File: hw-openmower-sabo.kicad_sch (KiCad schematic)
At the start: 31 parts, among them J1 Conn_01x05_Pin, J19 Conn_01x02, J20 Conn_01x02, J31 Conn_01x03_Pin, J32 Conn_02x08_Odd_Even, J33 Molex 470531000, M1 Fan, M2 Fan, Q4 AO3400A, Q5 AO3400A, U44 INA293A1, U7 M24C02-WMN

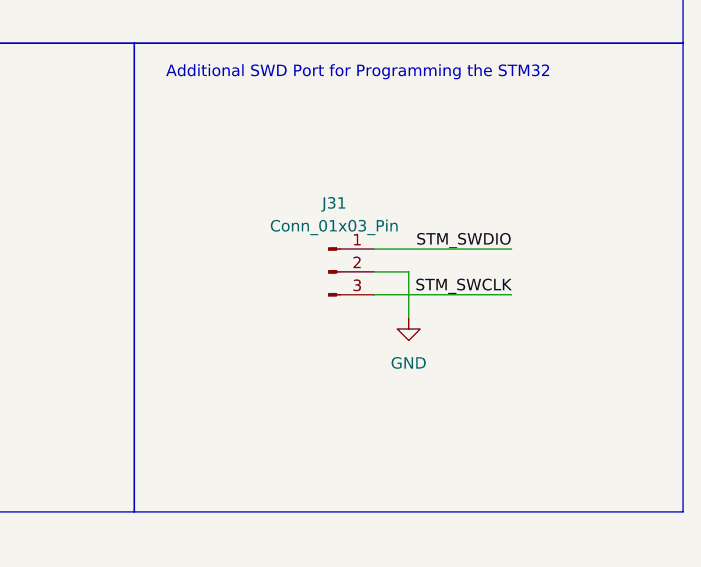
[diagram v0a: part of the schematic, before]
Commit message: - Increase charger Vfb
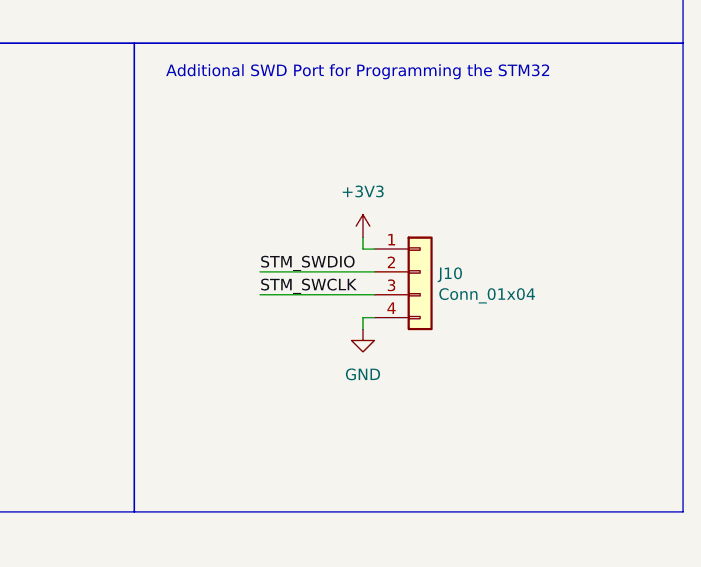
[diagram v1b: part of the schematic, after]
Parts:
- removed J31: Conn_01x03_Pin, Connector_PinHeader_2.54mm:PinHeader_1x03_P2.54mm_Vertical, symbol Connector:Conn_01x03_Pin
- added J10: Conn_01x04, Connector_JST:JST_XH_B4B-XH-A_1x04_P2.50mm_Vertical, symbol Connector_Generic:Conn_01x04
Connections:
- net +3V3: now also J10.1 (Pin_1)
- net GND: now also J10.4 (Pin_4)
- net STM_SWCLK: now also J10.3 (Pin_3)
- net STM_SWDIO: now also J10.2 (Pin_2)

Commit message: Change USS plugs and level shifter
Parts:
- removed Q5: AO3400A, Package_TO_SOT_SMD:SOT-23, symbol Transistor_FET:BSS138
- added Q5: AO3400A, Package_TO_SOT_SMD:SOT-23, symbol Transistor_FET:AO3400A
- Q4: symbol Transistor_FET:BSS138 -> Transistor_FET:AO3400A; Digikey BSS138K-13DICT-ND -> (none); Stock_PN Q-AP2300 -> (none)
- R9: footprint Resistor_SMD:R_0603_1608Metric_Pad0.98x0.95mm_HandSolder -> Resistor_SMD:R_0603_1608Metric
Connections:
- net GND: now also Q5.2 (S)
- net at D25.2 (A), M2.2 (-): now also Q5.3 (D)
- net at R65.2: now also Q5.1 (G)
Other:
- note added: "PG4 PG5 PG8 PD10"
- note added: "TIM1_CH1 TIM1_CH2 TIM1_CH3 TIM1_CH4 TIM15_CH1"
- note removed: "PWM Capable PE5 (Timer 9, Channel 2)"

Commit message: Add solder jumper to SWDIO- VTref
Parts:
- added JP6: VTref, Jumper:SolderJumper-2_P1.3mm_Bridged_RoundedPad1.0x1.5mm, symbol Jumper:Jumper_2_Bridged
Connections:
- net +3V3: now also JP6.1 (A); no longer J10.1 (Pin_1)
- new net: J10.1 (Pin_1), JP6.2 (B)
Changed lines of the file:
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@@
 		)
 	)
-	(wire
-		(pts
-			(xy 369.57 189.23) (xy 369.57 190.5)
-		)
-		(stroke
-			(width 0)
-			(type default)
-		)
-	)
 	(bus
 		(pts
@@
 	)
 	(symbol
+		(lib_id "Jumper:Jumper_2_Bridged")
+		(at 369.57 185.42 270)
+		(unit 1)
+		(body_style 1)
+		(exclude_from_sim no)
+		(in_bom yes)
+		(on_board yes)
+		(in_pos_files yes)
+		(dnp no)
+		(fields_autoplaced yes)
+		(property "Reference" "JP6"
+			(at 372.11 184.1499 90)
+			(show_name no)
+			(do_not_autoplace no)
+			(effects
+				(font
+					(size 1.27 1.27)
+				)
+				(justify left)
+			)
+		)
+		(property "Value" "VTref"
+			(at 372.11 186.6899 90)
+			(show_name no)
+			(do_not_autoplace no)
+			(effects
+				(font
+					(size 1.27 1.27)
+				)
+				(justify left)
+			)
+		)
+		(property "Footprint" "Jumper:SolderJumper-2_P1.3mm_Bridged_RoundedPad1.0x1.5mm"
+			(at 369.57 185.42 0)
+			(hide yes)
+			(show_name no)
+			(do_not_autoplace no)
+			(effects
+				(font
+					(size 1.27 1.27)
+				)
+			)
+		)
+		(property "Datasheet" ""
+			(at 364.49 185.42 0)
+			(hide yes)
+			(show_name no)
+			(do_not_autoplace no)
+			(effects
+				(font
+					(size 1.27 1.27)
+				)
+			)
+		)
+		(property "Description" "Jumper, 2-pole, closed/bridged"
+			(at 361.95 185.42 0)
+			(hide yes)
+			(show_name no)
+			(do_not_autoplace no)
+			(effects
+				(font
+					(size 1.27 1.27)
+				)
+			)
+		)
+		(pin "1"
+		)
+		(pin "2"
+		)
+		(instances
+			(project "hw-openmower-sabo"
+				(path "/e12e8a63-1d1b-4736-9aba-a87a258b2b11"
+					(reference "JP6")
+					(unit 1)
+				)
+			)
+		)
+	)
+	(symbol
 		(lib_id "Transistor_FET:AO3400A")
 		(at 294.64 90.17 0)
@@
 	(symbol
 		(lib_id "power:+3V3")
-		(at 369.57 189.23 0)
+		(at 369.57 180.34 0)
 		(unit 1)
 		(body_style 1)
@@
 		(fields_autoplaced yes)
 		(property "Reference" "#PWR0147"
-			(at 369.57 193.04 0)
+			(at 369.57 184.15 0)
 			(hide yes)
 			(show_name no)
@@
 		)
 		(property "Value" "+3V3"
-			(at 369.57 184.15 0)
+			(at 369.57 175.26 0)
 			(show_name no)
 			(do_not_autoplace no)
@@
 		)
 		(property "Footprint" ""
-			(at 369.57 189.23 0)
+			(at 369.57 180.34 0)
 			(hide yes)
 			(show_name no)
@@
 		)
 		(property "Datasheet" ""
-			(at 369.57 189.23 0)
+			(at 369.57 180.34 0)
 			(hide yes)
 			(show_name no)
@@
 		)
 		(property "Description" "Power symbol creates a global label with name \"+3V3\""
-			(at 369.57 189.23 0)
+			(at 369.57 180.34 0)
 			(hide yes)
 			(show_name no)

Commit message: Production preparation
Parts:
- J10: DNP Y -> (none); Digikey 455-2249-ND -> (none); LCSC Part # (none) -> C7429634; Stock_PN J-JST-XH-1x4 -> (none)
